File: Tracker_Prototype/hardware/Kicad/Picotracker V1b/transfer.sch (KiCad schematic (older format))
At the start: 35 parts, among them J1 Conn_01x06, J2 GND, J3 3.3V, SW1 SW_Push, U1 MAX-M8C, U3 CMWX1ZZABZ-078, U6 MS5607-02BA

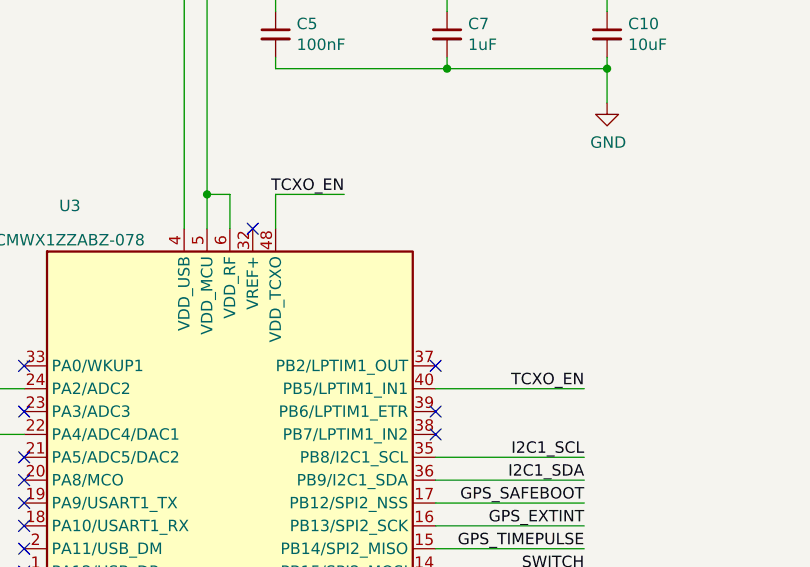
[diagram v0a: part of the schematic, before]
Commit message: updated circuit of b variant for low power voltage measurment. Made a variant tcxo enable controllable
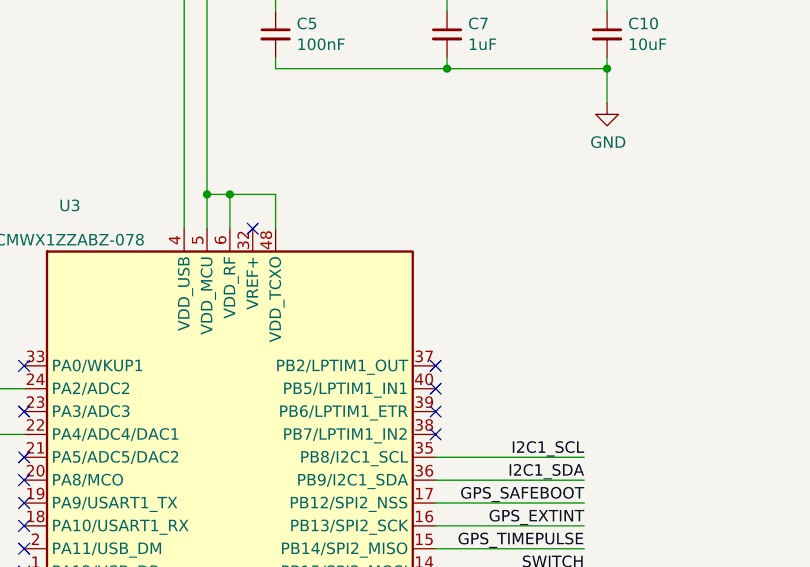
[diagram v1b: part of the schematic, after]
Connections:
- net labels removed: TCXO_EN
- wire segments 133 -> 132
- no-connect marks 32 -> 33
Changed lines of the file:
@@
 $Descr A3 16535 11693
 encoding utf-8
-Sheet 1 1
+Sheet 2 2
 Title "Pico lora tracker"
 Date "2019-10-21"
@@
 AR Path="/5D5B15F7/5DC84019" Ref="#PWR?"  Part="1"
 AR Path="/5DC84019" Ref="#PWR0101"  Part="1"
+AR Path="/5E01805B/5DC84019" Ref="#PWR0101"  Part="1"
 F 0 "#PWR0101" H 6250 5500 50  0001 C CNN
 F 1 "GND" H 6255 5577 50  0000 C CNN
@@
 AR Path="/5D5B15F7/5DC84030" Ref="#PWR?"  Part="1"
 AR Path="/5DC84030" Ref="#PWR0103"  Part="1"
+AR Path="/5E01805B/5DC84030" Ref="#PWR0103"  Part="1"
 F 0 "#PWR0103" H 5000 5500 50  0001 C CNN
 F 1 "GND" H 5005 5577 50  0000 C CNN
@@
 AR Path="/5D5B15F7/5DC8403F" Ref="#PWR?"  Part="1"
 AR Path="/5DC8403F" Ref="#PWR0104"  Part="1"
+AR Path="/5E01805B/5DC8403F" Ref="#PWR0104"  Part="1"
 F 0 "#PWR0104" H 1750 1100 50  0001 C CNN
 F 1 "+3.3V" H 1765 1423 50  0000 C CNN
@@
 AR Path="/5D5B15F7/5DC84056" Ref="#PWR?"  Part="1"
 AR Path="/5DC84056" Ref="#PWR0105"  Part="1"
+AR Path="/5E01805B/5DC84056" Ref="#PWR0105"  Part="1"
 F 0 "#PWR0105" H 1750 2000 50  0001 C CNN
 F 1 "GND" H 1755 2077 50  0000 C CNN
@@
 AR Path="/5D5B15F7/5DC84068" Ref="#PWR?"  Part="1"
 AR Path="/5DC84068" Ref="#PWR0106"  Part="1"
+AR Path="/5E01805B/5DC84068" Ref="#PWR0106"  Part="1"
 F 0 "#PWR0106" H 4550 4650 50  0001 C CNN
 F 1 "GND" H 4555 4727 50  0000 C CNN
@@
 AR Path="/5D5B15F7/5DC8408D" Ref="#PWR?"  Part="1"
 AR Path="/5DC8408D" Ref="#PWR0107"  Part="1"
+AR Path="/5E01805B/5DC8408D" Ref="#PWR0107"  Part="1"
 F 0 "#PWR0107" H 7900 900 50  0001 C CNN
 F 1 "+3.3V" H 7915 1223 50  0000 C CNN
@@
 AR Path="/5D5B15F7/5DC840A2" Ref="#PWR?"  Part="1"
 AR Path="/5DC840A2" Ref="#PWR0108"  Part="1"
+AR Path="/5E01805B/5DC840A2" Ref="#PWR0108"  Part="1"
 F 0 "#PWR0108" H 7900 1600 50  0001 C CNN
 F 1 "GND" H 7905 1677 50  0000 C CNN
@@
 AR Path="/5D5B15F7/5DC840D7" Ref="#PWR?"  Part="1"
 AR Path="/5DC840D7" Ref="#PWR0111"  Part="1"
+AR Path="/5E01805B/5DC840D7" Ref="#PWR0111"  Part="1"
 F 0 "#PWR0111" H 7550 5500 50  0001 C CNN
 F 1 "GND" H 7555 5577 50  0000 C CNN
@@
 AR Path="/5D5B15F7/5DC840DE" Ref="#PWR?"  Part="1"
 AR Path="/5DC840DE" Ref="#PWR0112"  Part="1"
+AR Path="/5E01805B/5DC840DE" Ref="#PWR0112"  Part="1"
 F 0 "#PWR0112" H 8100 5500 50  0001 C CNN
 F 1 "GND" H 8105 5577 50  0000 C CNN
@@
 AR Path="/5D5B15F7/5DC840FF" Ref="#PWR?"  Part="1"
 AR Path="/5DC840FF" Ref="#PWR0113"  Part="1"
+AR Path="/5E01805B/5DC840FF" Ref="#PWR0113"  Part="1"
 F 0 "#PWR0113" H 14650 3600 50  0001 C CNN
 F 1 "GND" H 14655 3677 50  0000 C CNN
@@
 AR Path="/5D5B15F7/5DC84105" Ref="#PWR?"  Part="1"
 AR Path="/5DC84105" Ref="#PWR0114"  Part="1"
+AR Path="/5E01805B/5DC84105" Ref="#PWR0114"  Part="1"
 F 0 "#PWR0114" H 14050 3600 50  0001 C CNN
 F 1 "GND" H 14055 3677 50  0000 C CNN
@@
 AR Path="/5D5B15F7/5DC84110" Ref="#PWR?"  Part="1"
 AR Path="/5DC84110" Ref="#PWR0115"  Part="1"
+AR Path="/5E01805B/5DC84110" Ref="#PWR0115"  Part="1"
 F 0 "#PWR0115" H 15100 2750 50  0001 C CNN
 F 1 "GND" H 15105 2827 50  0000 C CNN
@@
 AR Path="/5D5B15F7/5DC84121" Ref="#PWR?"  Part="1"
 AR Path="/5DC84121" Ref="#PWR0116"  Part="1"
+AR Path="/5E01805B/5DC84121" Ref="#PWR0116"  Part="1"
 F 0 "#PWR0116" H 14650 2550 50  0001 C CNN
 F 1 "+3.3V" H 14665 2873 50  0000 C CNN
@@
 AR Path="/5D5B15F7/5DC84141" Ref="#PWR?"  Part="1"
 AR Path="/5DC84141" Ref="#PWR0117"  Part="1"
+AR Path="/5E01805B/5DC84141" Ref="#PWR0117"  Part="1"
 F 0 "#PWR0117" H 12700 900 50  0001 C CNN
 F 1 "+3.3V" H 12715 1223 50  0000 C CNN
@@
 AR Path="/5D5B15F7/5DC84147" Ref="#PWR?"  Part="1"
 AR Path="/5DC84147" Ref="#PWR0118"  Part="1"
+AR Path="/5E01805B/5DC84147" Ref="#PWR0118"  Part="1"
 F 0 "#PWR0118" H 13000 900 50  0001 C CNN
 F 1 "+3.3V" H 13015 1223 50  0000 C CNN
@@
 AR Path="/5D5B15F7/5DC84165" Ref="#PWR?"  Part="1"
 AR Path="/5DC84165" Ref="#PWR0119"  Part="1"
+AR Path="/5E01805B/5DC84165" Ref="#PWR0119"  Part="1"
 F 0 "#PWR0119" H 13550 8100 50  0001 C CNN
 F 1 "GND" H 13555 8177 50  0000 C CNN
@@
 AR Path="/5D5B15F7/5DC841BA" Ref="#PWR?"  Part="1"
 AR Path="/5DC841BA" Ref="#PWR0122"  Part="1"
+AR Path="/5E01805B/5DC841BA" Ref="#PWR0122"  Part="1"
 F 0 "#PWR0122" H 13350 5400 50  0001 C CNN
 F 1 "+3.3V" H 13365 5723 50  0000 C CNN
@@
 AR Path="/5D5B15F7/5DC841DF" Ref="#PWR?"  Part="1"
 AR Path="/5DC841DF" Ref="#PWR0123"  Part="1"
+AR Path="/5E01805B/5DC841DF" Ref="#PWR0123"  Part="1"
 F 0 "#PWR0123" H 12800 6350 50  0001 C CNN
 F 1 "GND" H 12805 6427 50  0000 C CNN
@@
 AR Path="/5D5B15F7/5DFABE1F" Ref="#PWR?"  Part="1"
 AR Path="/5DFABE1F" Ref="#PWR0121"  Part="1"
+AR Path="/5E01805B/5DFABE1F" Ref="#PWR0121"  Part="1"
 F 0 "#PWR0121" H 11750 7350 50  0001 C CNN
 F 1 "+3.3V" H 11765 7673 50  0000 C CNN
@@
 AR Path="/5D5B15F7/5DC84013" Ref="U?"  Part="1"
 AR Path="/5DC84013" Ref="U3"  Part="1"
+AR Path="/5E01805B/5DC84013" Ref="U3"  Part="1"
 F 0 "U3" H 5550 5500 50  0000 C CNN
 F 1 "CMWX1ZZABZ-078" H 5550 5350 50  0000 C CNN
@@
 AR Path="/5D5B15F7/5DC841D3" Ref="C?"  Part="1"
 AR Path="/5DC841D3" Ref="C13"  Part="1"
+AR Path="/5E01805B/5DC841D3" Ref="C13"  Part="1"
 F 0 "C13" H 13058 6346 50  0000 R CNN
 F 1 "10uF" H 13058 6255 50  0000 R CNN
@@
 AR Path="/5D5B15F7/5DC841CA" Ref="C?"  Part="1"
 AR Path="/5DC841CA" Ref="C12"  Part="1"
+AR Path="/5E01805B/5DC841CA" Ref="C12"  Part="1"
 F 0 "C12" H 12708 6346 50  0000 R CNN
 F 1 "100nF" H 12708 6255 50  0000 R CNN
@@
 AR Path="/5D5B15F7/5DC8415A" Ref="R?"  Part="1"
 AR Path="/5DC8415A" Ref="R5"  Part="1"
+AR Path="/5E01805B/5DC8415A" Ref="R5"  Part="1"
 F 0 "R5" H 13070 1596 50  0000 L CNN
 F 1 "4.7K" H 13070 1505 50  0000 L CNN
@@
 AR Path="/5D5B15F7/5DC84150" Ref="R?"  Part="1"
 AR Path="/5DC84150" Ref="R4"  Part="1"
+AR Path="/5E01805B/5DC84150" Ref="R4"  Part="1"
 F 0 "R4" H 12770 1596 50  0000 L CNN
 F 1 "4.7K" H 12770 1505 50  0000 L CNN
@@
 AR Path="/5D5B15F7/5DC84133" Ref="C?"  Part="1"
 AR Path="/5DC84133" Ref="C14"  Part="1"
+AR Path="/5E01805B/5DC84133" Ref="C14"  Part="1"
 F 0 "C14" H 15192 2896 50  0000 L CNN
 F 1 "220nF" H 15192 2805 50  0000 L CNN
@@
 AR Path="/5D5B15F7/5DC8412A" Ref="U?"  Part="1"
 AR Path="/5DC8412A" Ref="U6"  Part="1"
+AR Path="/5E01805B/5DC8412A" Ref="U6"  Part="1"
 F 0 "U6" H 14980 3346 50  0000 L CNN
 F 1 "MS5607-02BA" H 14980 3255 50  0000 L CNN
@@
 AR Path="/5D5B15F7/5DC840F4" Ref="L?"  Part="1"
 AR Path="/5DC840F4" Ref="L1"  Part="1"
+AR Path="/5E01805B/5DC840F4" Ref="L1"  Part="1"
 F 0 "L1" V 7619 5200 50  0000 C CNN
 F 1 "NF" V 7710 5200 50  0000 C CNN
@@
 AR Path="/5D5B15F7/5DC840ED" Ref="C?"  Part="1"
 AR Path="/5DC840ED" Ref="C11"  Part="1"
+AR Path="/5E01805B/5DC840ED" Ref="C11"  Part="1"
 F 0 "C11" H 8192 5546 50  0000 L CNN
 F 1 "NF" H 8192 5455 50  0000 L CNN
@@
 AR Path="/5D5B15F7/5DC840E6" Ref="C?"  Part="1"
 AR Path="/5DC840E6" Ref="C9"  Part="1"
+AR Path="/5E01805B/5DC840E6" Ref="C9"  Part="1"
 F 0 "C9" H 7642 5546 50  0000 L CNN
 F 1 "NF" H 7642 5455 50  0000 L CNN
@@
 AR Path="/5D5B15F7/5DC8409B" Ref="C?"  Part="1"
 AR Path="/5DC8409B" Ref="C10"  Part="1"
+AR Path="/5E01805B/5DC8409B" Ref="C10"  Part="1"
 F 0 "C10" H 7992 1596 50  0000 L CNN
 F 1 "10uF" H 7992 1505 50  0000 L CNN
@@
 AR Path="/5D5B15F7/5DC84094" Ref="C?"  Part="1"
 AR Path="/5DC84094" Ref="C7"  Part="1"
+AR Path="/5E01805B/5DC84094" Ref="C7"  Part="1"
 F 0 "C7" H 7292 1596 50  0000 L CNN
 F 1 "1uF" H 7292 1505 50  0000 L CNN
@@
 AR Path="/5D5B15F7/5DC84080" Ref="C?"  Part="1"
 AR Path="/5DC84080" Ref="C5"  Part="1"
+AR Path="/5E01805B/5DC84080" Ref="C5"  Part="1"
 F 0 "C5" H 6542 1596 50  0000 L CNN
 F 1 "100nF" H 6542 1505 50  0000 L CNN
@@
 AR Path="/5D5B15F7/5DC8406E" Ref="C?"  Part="1"
 AR Path="/5DC8406E" Ref="C1"  Part="1"
+AR Path="/5E01805B/5DC8406E" Ref="C1"  Part="1"
 F 0 "C1" H 4642 4696 50  0000 L CNN
 F 1 "100nF" H 4642 4605 50  0000 L CNN
@@
 AR Path="/5D5B15F7/5DC84045" Ref="J?"  Part="1"
 AR Path="/5DC84045" Ref="J1"  Part="1"
+AR Path="/5E01805B/5DC84045" Ref="J1"  Part="1"
 F 0 "J1" H 1068 2167 50  0000 C CNN
 F 1 "Conn_01x06" H 1068 2076 50  0000 C CNN
@@
 AR Path="/5D5B15F7/5DC84036" Ref="R?"  Part="1"
 AR Path="/5DC84036" Ref="R3"  Part="1"
+AR Path="/5E01805B/5DC84036" Ref="R3"  Part="1"
 F 0 "R3" H 5070 5496 50  0000 L CNN
 F 1 "10K" H 5070 5405 50  0000 L CNN
@@
 AR Path="/5D5B15F7/5DB685A2" Ref="#PWR?"  Part="1"
 AR Path="/5DB685A2" Ref="#PWR0124"  Part="1"
+AR Path="/5E01805B/5DB685A2" Ref="#PWR0124"  Part="1"
 F 0 "#PWR0124" H 14250 7100 50  0001 C CNN
 F 1 "GND" H 14350 7350 50  0000 C CNN
@@
 AR Path="/5D5B15F7/5DC840B0" Ref="#PWR?"  Part="1"
 AR Path="/5DC840B0" Ref="#PWR0109"  Part="1"
+AR Path="/5E01805B/5DC840B0" Ref="#PWR0109"  Part="1"
 F 0 "#PWR0109" H 4750 900 50  0001 C CNN
 F 1 "+3.3V" H 4765 1223 50  0000 C CNN
@@
 AR Path="/5D5B15F7/5DBBC44F" Ref="#PWR?"  Part="1"
 AR Path="/5DBBC44F" Ref="#PWR02"  Part="1"
+AR Path="/5E01805B/5DBBC44F" Ref="#PWR02"  Part="1"
 F 0 "#PWR02" H 10850 4000 50  0001 C CNN
 F 1 "GND" H 10855 4077 50  0000 C CNN
@@
 AR Path="/5D5B15F7/5DC040B5" Ref="#PWR?"  Part="1"
 AR Path="/5DC040B5" Ref="#PWR03"  Part="1"
+AR Path="/5E01805B/5DC040B5" Ref="#PWR03"  Part="1"
 F 0 "#PWR03" H 9900 6150 50  0001 C CNN
 F 1 "GND" H 9905 6227 50  0000 C CNN
@@
 AR Path="/5D5B15F7/5DC0A475" Ref="#PWR?"  Part="1"
 AR Path="/5DC0A475" Ref="#PWR04"  Part="1"
+AR Path="/5E01805B/5DC0A475" Ref="#PWR04"  Part="1"
 F 0 "#PWR04" H 10750 5150 50  0001 C CNN
 F 1 "+3.3V" H 10765 5473 50  0000 C CNN
@@
 Text Notes 7100 9100 0    50   ~ 0
 Structural holes\n
+Wire Wire Line
+	6450 2250 6250 2250
+Connection ~ 6250 2250
+NoConn ~ 7150 3100
 NoConn ~ 7150 3200
-Wire Wire Line
-	6450 2250 6750 2250
-Text Label 6750 2250 2    50   ~ 0
-TCXO_EN
-Text Label 7800 3100 2    50   ~ 0
-TCXO_EN
-Wire Wire Line
-	7150 3100 7800 3100
 $EndSCHEMATC
